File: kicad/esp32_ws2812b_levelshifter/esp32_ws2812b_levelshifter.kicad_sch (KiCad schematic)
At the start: 8 parts, among them J1 ESP32, J2 WS2812B, J3 PWR_5V, U1 SN74HCT245

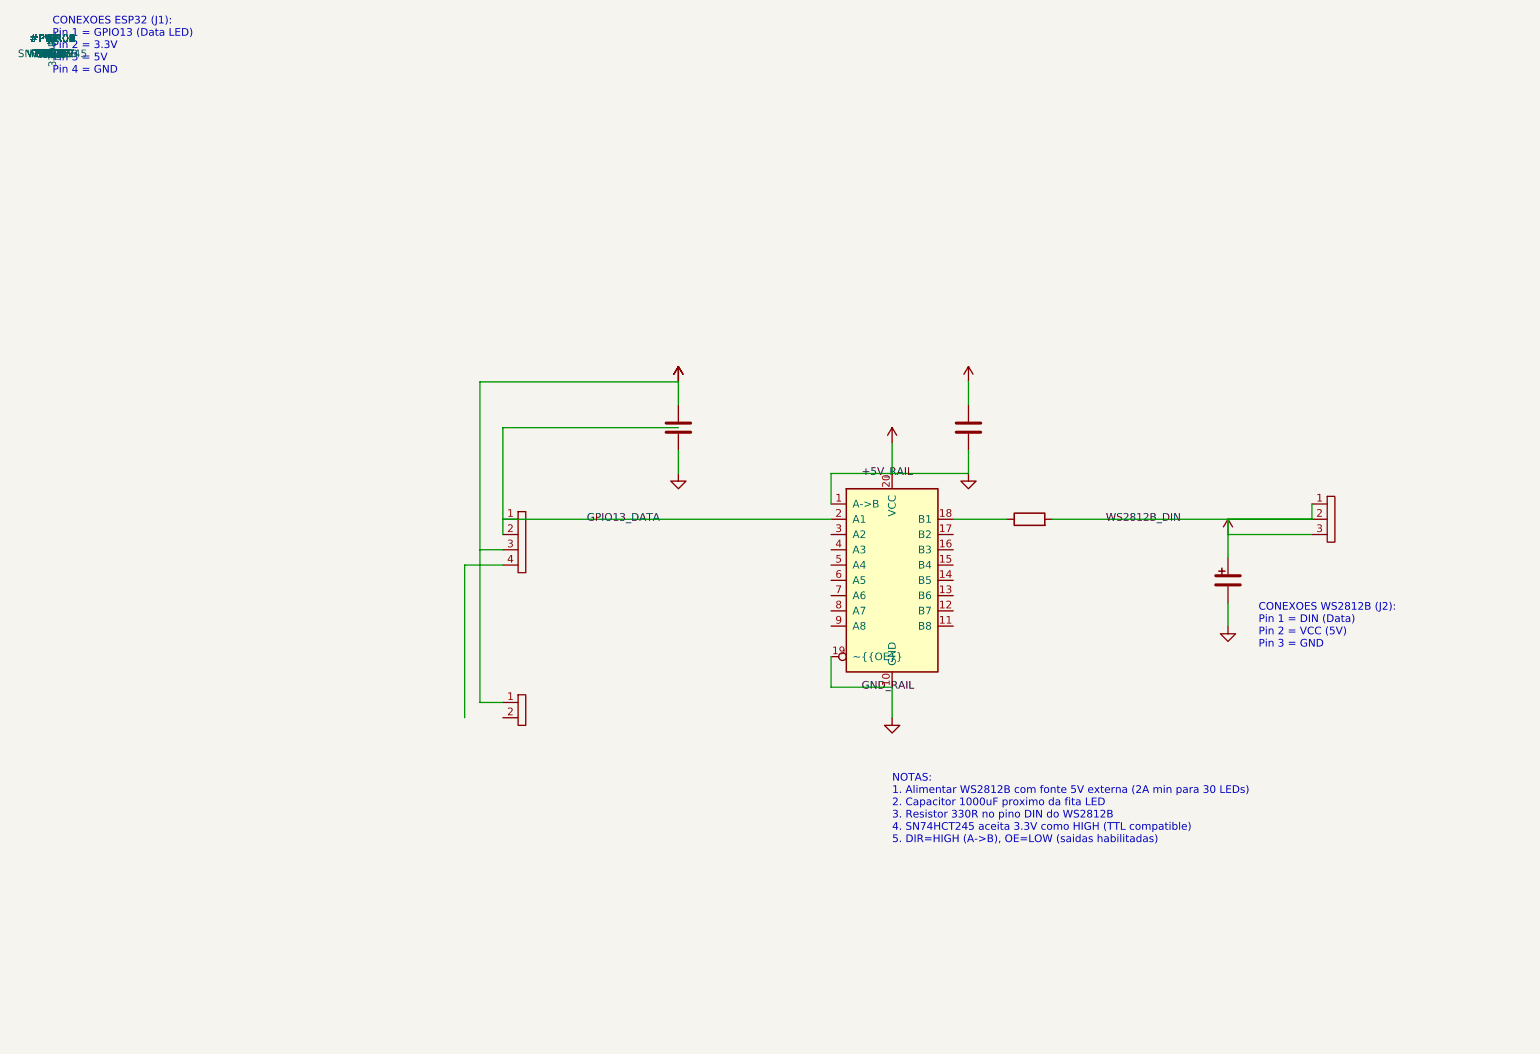
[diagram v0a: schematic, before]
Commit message: refactor: update to SN74HCT125 (DIP-14) per user schematic
- Replace SN74HCT245 (DIP-20) with SN74HCT125 (DIP-14, quad buffer)
- All ~OE pins tied to GND (outputs always enabled)
- Channel 1: GPIO13 -> 1A (pin2) -> 1Y (pin3) -> R1 -> WS2812B DIN
- Resistor changed from 330R to 62-100R per reference schematic
- 100nF bypass cap between VCC (pin14) and GND (pin7)
- PCB reduced to 40x30mm (smaller IC footprint)
- Updated BOM and documentation

Co-Authored-By: josefrizi@gmail.com <josefrizi@gmail.com>
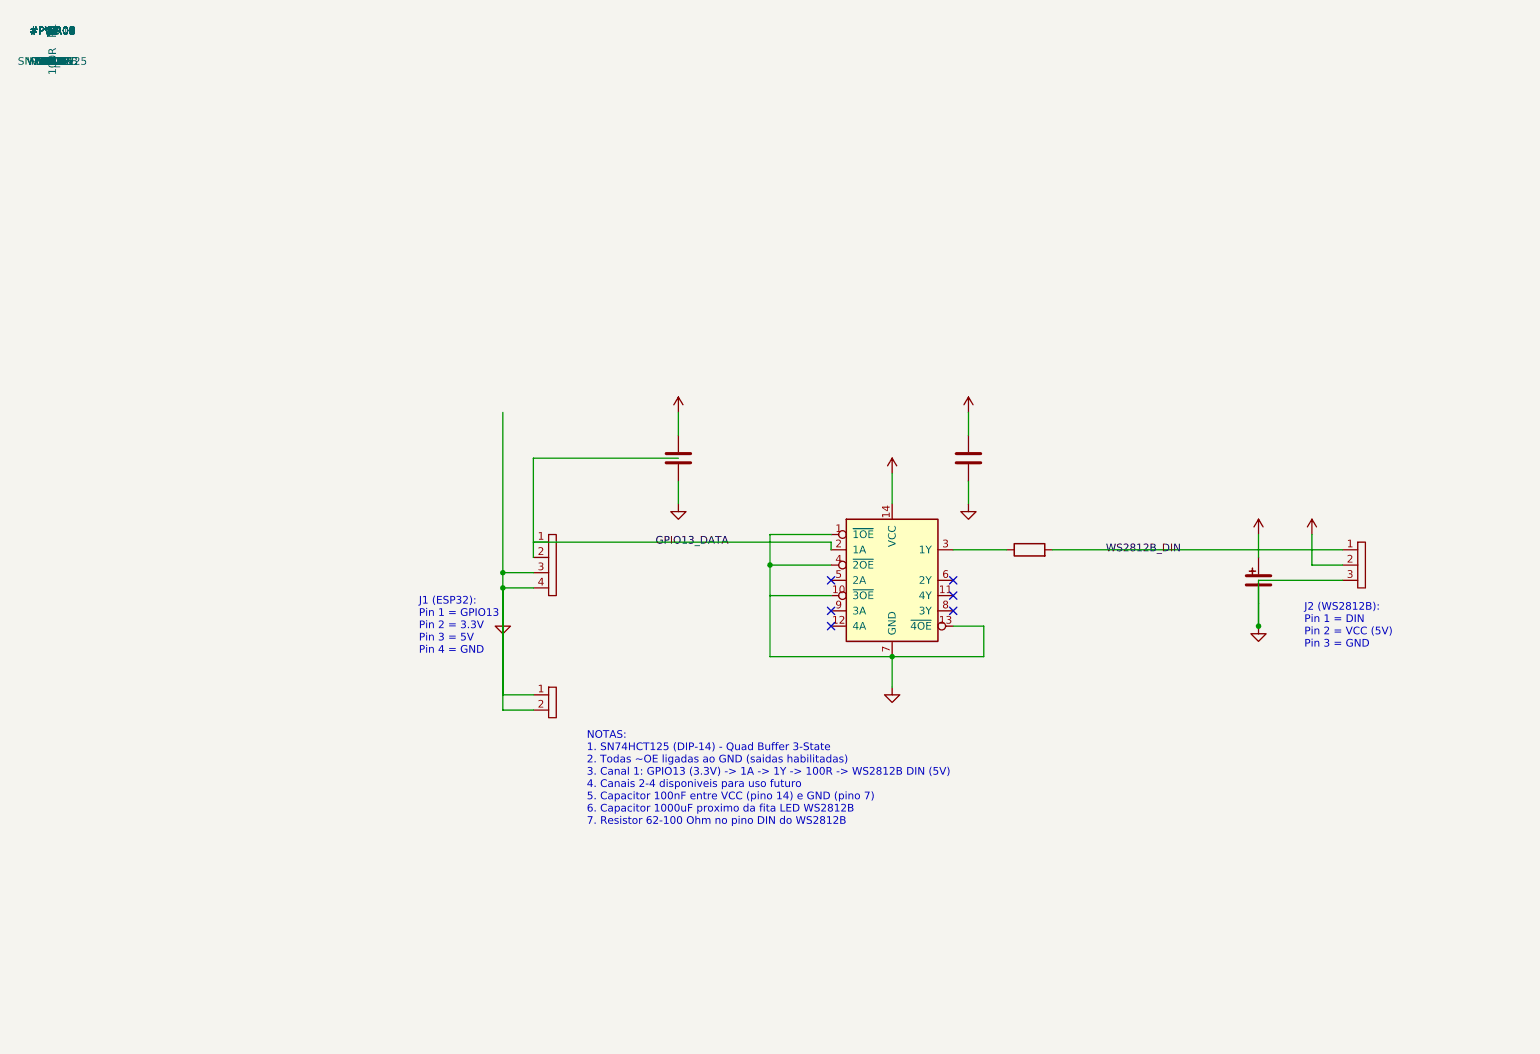
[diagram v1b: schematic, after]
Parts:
- removed U1: SN74HCT245, symbol 74xx:74HCT245
- added U1: SN74HCT125, symbol 74xx:74HCT125
- R1: value 330R -> 100R
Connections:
- net +3V3: no longer C1.1, C1.2, C2.1, C2.2, C3.2, J1.3 (Pin_3), J2.1 (Pin_1), J2.2 (Pin_2), J2.3 (Pin_3), J3.1 (Pin_1), R1.2
- net GPIO13_DATA: now also U1.2 (1A)
- net GND: now reaches J3.2 (Pin_2)
- net GND: now also C1.2, C2.2, C3.2, J1.3 (Pin_3), J1.4 (Pin_4), J2.3 (Pin_3), J3.1 (Pin_1), U1.1 (~{1OE}), U1.10 (~{3OE}), U1.13 (~{4OE}), U1.4 (~{2OE}), U1.7 (GND)
- net at R1.1: now also U1.3 (1Y)
- new net +5V: C1.1, C2.1, J2.2 (Pin_2), U1.14 (VCC)
- new net WS2812B_DIN: J2.1 (Pin_1), R1.2
- no-connect marks 0 -> 6
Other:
- note added: "J1 (ESP32): Pin 1 = GPIO13 Pin 2 = 3.3V Pin 3 = 5V Pin 4 = GND"
- note added: "J2 (WS2812B): Pin 1 = DIN Pin 2 = VCC (5V) Pin 3 = GND"
- note added: "NOTAS: 1. SN74HCT125 (DIP-14) - Quad Buffer 3-State 2. Todas ~OE ligadas ao GND (saidas habilitadas) 3. Canal 1: GPIO13 (3.3V) -> 1A -> 1Y -> 100R -> WS2812B DIN (5V) 4. Canais 2-4 disponiveis para uso futuro 5. Capacitor 100nF entre VCC (pino 14) e GND (pino 7) 6. Capacitor 1000uF proximo da fita LED WS2812B 7. Resistor 62-100 Ohm no pino DIN do WS2812B"
- note removed: "CONEXOES ESP32 (J1): Pin 1 = GPIO13 (Data LED) Pin 2 = 3.3V Pin 3 = 5V Pin 4 = GND"
- note removed: "CONEXOES WS2812B (J2): Pin 1 = DIN (Data) Pin 2 = VCC (5V) Pin 3 = GND"
- note removed: "NOTAS: 1. Alimentar WS2812B com fonte 5V externa (2A min para 30 LEDs) 2. Capacitor 1000uF proximo da fita LED 3. Resistor 330R no pino DIN do WS2812B 4. SN74HCT245 aceita 3.3V como HIGH (TTL compatible) 5. DIR=HIGH (A->B), OE=LOW (saidas habilitadas)"
- title: ESP32 + SN74HCT245 Level Shifter para WS2812B -> ESP32 + SN74HCT125 Level Shifter para WS2812B

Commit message: fix: use official KiCad multi-unit symbol format for SN74HCT125
- Symbol now uses 5 units (4 gates + power) matching KiCad 74xx library format
- Each gate drawn as triangle buffer with ~OE, A input, Y output
- Unit 5 contains VCC (pin 14) and GND (pin 7) in rectangle
- Fixes symbol loading issue in KiCad 10
- Matches official 74LS125 symbol structure (74HCT125 extends 74LS125)

Co-Authored-By: josefrizi@gmail.com <josefrizi@gmail.com>
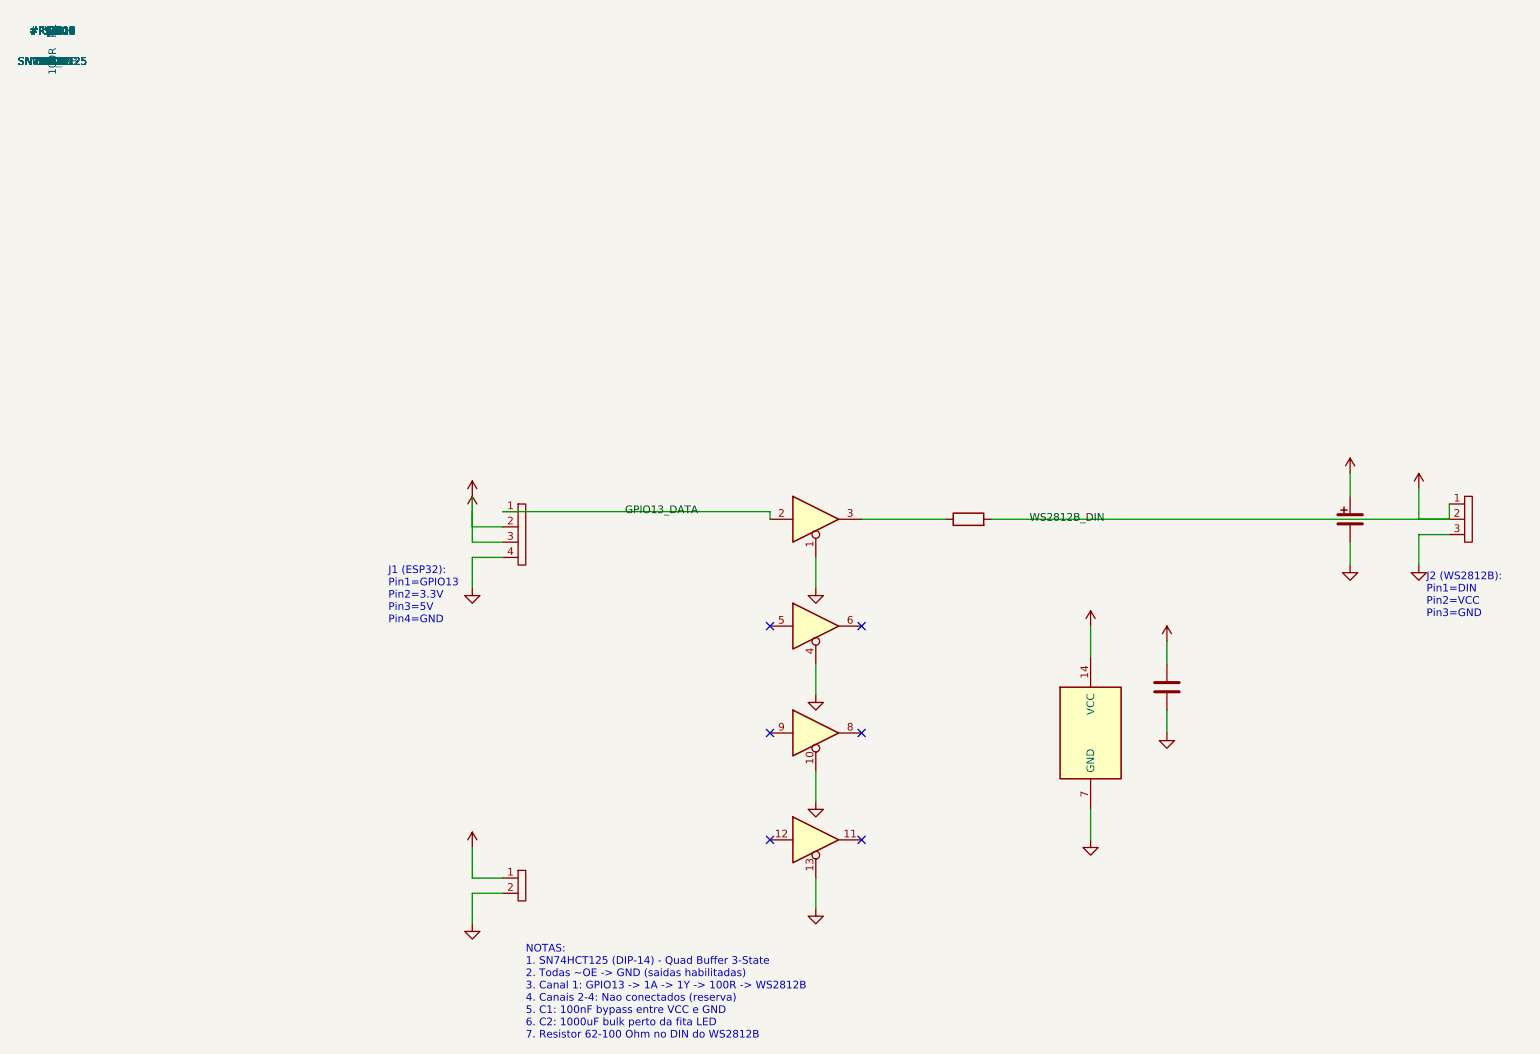
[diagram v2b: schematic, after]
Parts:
- removed C3: 100nF, symbol Device:C
- added unit 4 of U1
- added unit 5 of U1
- added unit 3 of U1
- added unit 2 of U1
- J3: value PWR_5V -> PWR_IN
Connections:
- net WS2812B_DIN is gone; now on net +3V3: J2.1 (Pin_1), R1.2
- net +3V3: now also C1.1, C2.1, J1.2 (Pin_2), J1.3 (Pin_3), J2.2 (Pin_2), J3.1 (Pin_1), U1.14 (VCC)
- net GND: now also U1.10, U1.13, U1.4, U1.7 (GND); no longer J1.3 (Pin_3), J3.1 (Pin_1), U1.10 (~{3OE}), U1.13 (~{4OE}), U1.4 (~{2OE}), U1.7 (GND)
- removed net +5V: C1.1, C2.1, J2.2 (Pin_2), U1.14 (VCC)
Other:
- note added: "J1 (ESP32): Pin1=GPIO13 Pin2=3.3V Pin3=5V Pin4=GND"
- note added: "J2 (WS2812B): Pin1=DIN Pin2=VCC Pin3=GND"
- note added: "NOTAS: 1. SN74HCT125 (DIP-14) - Quad Buffer 3-State 2. Todas ~OE -> GND (saidas habilitadas) 3. Canal 1: GPIO13 -> 1A -> 1Y -> 100R -> WS2812B 4. Canais 2-4: Nao conectados (reserva) 5. C1: 100nF bypass entre VCC e GND 6. C2: 1000uF bulk perto da fita LED 7. Resistor 62-100 Ohm no DIN do WS2812B"
- note removed: "J1 (ESP32): Pin 1 = GPIO13 Pin 2 = 3.3V Pin 3 = 5V Pin 4 = GND"
- note removed: "J2 (WS2812B): Pin 1 = DIN Pin 2 = VCC (5V) Pin 3 = GND"
- note removed: "NOTAS: 1. SN74HCT125 (DIP-14) - Quad Buffer 3-State 2. Todas ~OE ligadas ao GND (saidas habilitadas) 3. Canal 1: GPIO13 (3.3V) -> 1A -> 1Y -> 100R -> WS2812B DIN (5V) 4. Canais 2-4 disponiveis para uso futuro 5. Capacitor 100nF entre VCC (pino 14) e GND (pino 7) 6. Capacitor 1000uF proximo da fita LED WS2812B 7. Resistor 62-100 Ohm no pino DIN do WS2812B"

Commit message: fix: single-unit DIP-14 block symbol for SN74HCT125
- All 14 pins visible in one rectangle block (DIP-14 layout)
- Left side: pins 1-7 (~1OE, 1A, 1Y, ~2OE, 2A, 2Y, GND)
- Right side: pins 14-8 (VCC, ~4OE, 4A, 4Y, ~3OE, 3A, 3Y)
- Pin names with overbar notation: ~{1OE}, ~{2OE}, ~{3OE}, ~{4OE}
- IC shows as complete DIP-14 package in schematic

Co-Authored-By: josefrizi@gmail.com <josefrizi@gmail.com>
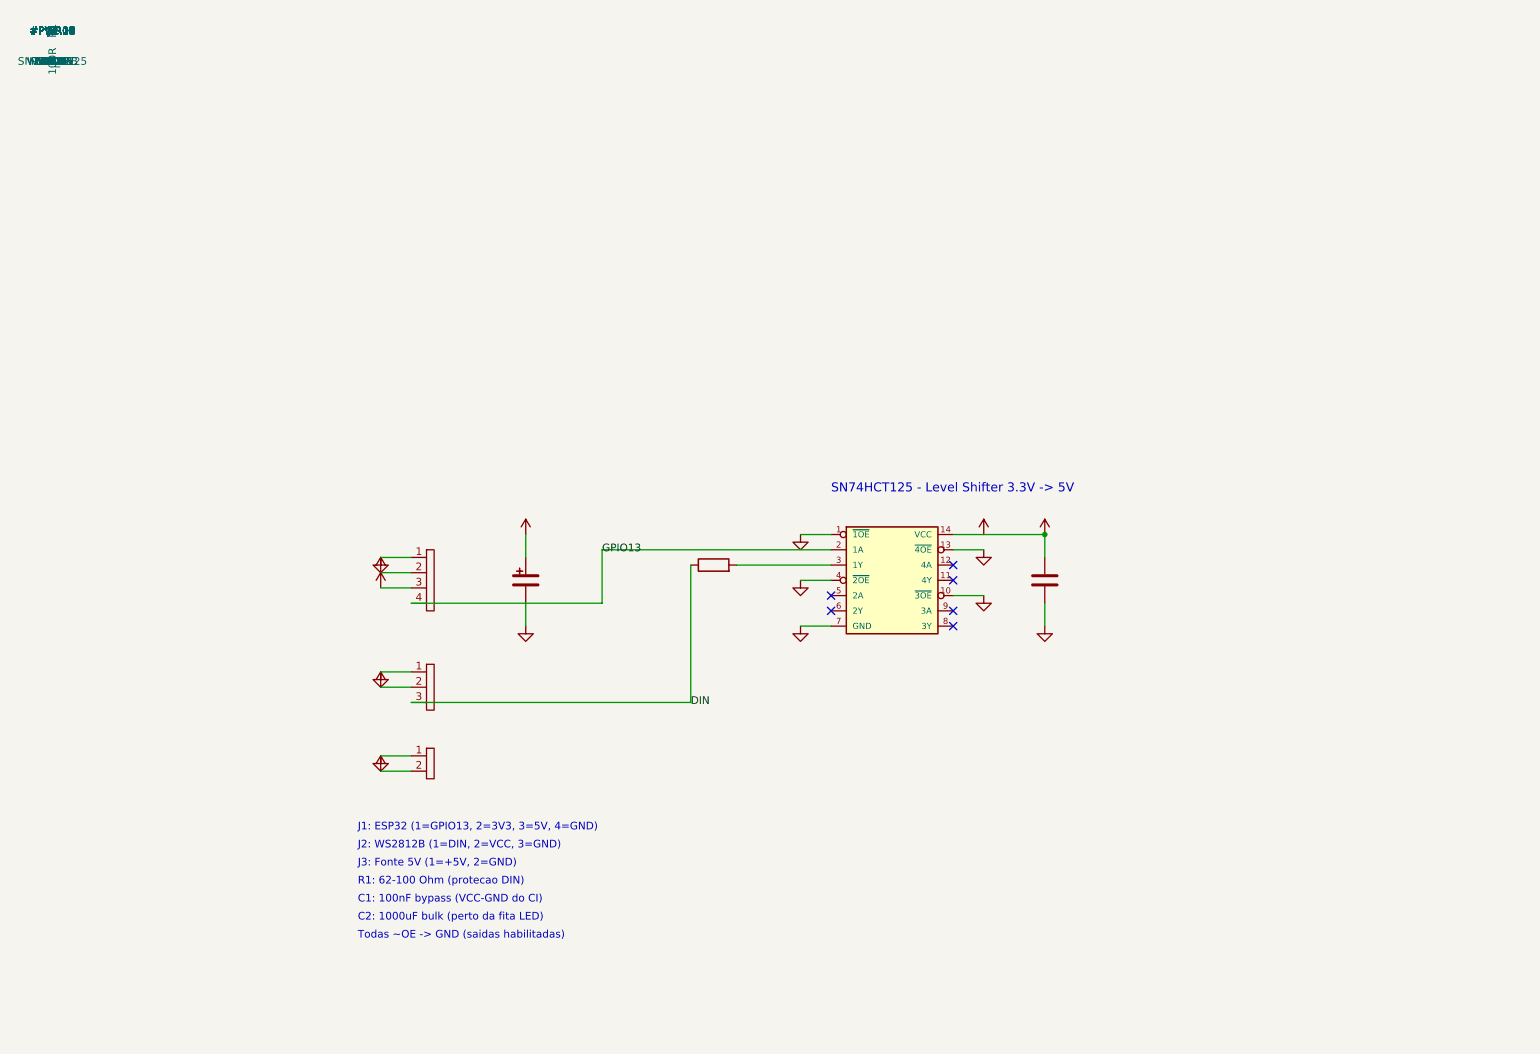
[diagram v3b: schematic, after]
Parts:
- removed unit 4 of U1
- removed unit 5 of U1
- removed unit 3 of U1
- removed unit 2 of U1
- C1: footprint (none) -> Capacitor_THT:C_Disc_D5.0mm_W2.5mm_P2.54mm
- C2: footprint (none) -> Capacitor_THT:CP_Radial_D8.0mm_P3.50mm
- J1: footprint (none) -> Connector_PinHeader_2.54mm:PinHeader_1x04_P2.54mm_Vertical
- J2: footprint (none) -> Connector_PinHeader_2.54mm:PinHeader_1x03_P2.54mm_Vertical
- J3: value PWR_IN -> PWR_5V; footprint (none) -> Connector_PinHeader_2.54mm:PinHeader_1x02_P2.54mm_Vertical
- R1: footprint (none) -> Resistor_THT:R_Axial_DIN0207_L6.3mm_D2.5mm_P10.16mm_Horizontal
- U1: footprint (none) -> Package_DIP:DIP-14_W7.62mm
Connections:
- net +3V3: no longer C1.1, C2.1, J1.2 (Pin_2), J2.1 (Pin_1), J2.2 (Pin_2), J3.1 (Pin_1), R1.2
- net GND: now also J1.1 (Pin_1), J2.1 (Pin_1), J3.1 (Pin_1), U1.10 (~{3OE}), U1.13 (~{4OE}), U1.4 (~{2OE}), U1.7 (GND); no longer J1.4 (Pin_4), J2.3 (Pin_3), J3.2 (Pin_2)
- net at U1.3 (1Y): now also R1.2; no longer R1.1
- net GPIO13_DATA renamed GPIO13
- net GPIO13: now also J1.4 (Pin_4); no longer J1.1 (Pin_1)
- new net +5V: C1.1, C2.1, J1.2 (Pin_2), J2.2 (Pin_2), J3.2 (Pin_2), U1.14 (VCC)
- new net DIN: J2.3 (Pin_3), R1.1
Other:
- note added: "C1: 100nF bypass (VCC-GND do CI)"
- note added: "C2: 1000uF bulk (perto da fita LED)"
- note added: "J1: ESP32 (1=GPIO13, 2=3V3, 3=5V, 4=GND)"
- note added: "J2: WS2812B (1=DIN, 2=VCC, 3=GND)"
- note added: "J3: Fonte 5V (1=+5V, 2=GND)"
- note added: "R1: 62-100 Ohm (protecao DIN)"
- note added: "SN74HCT125 - Level Shifter 3.3V -> 5V"
- note added: "Todas ~OE -> GND (saidas habilitadas)"
- note removed: "J1 (ESP32): Pin1=GPIO13 Pin2=3.3V Pin3=5V Pin4=GND"
- note removed: "J2 (WS2812B): Pin1=DIN Pin2=VCC Pin3=GND"
- note removed: "NOTAS: 1. SN74HCT125 (DIP-14) - Quad Buffer 3-State 2. Todas ~OE -> GND (saidas habilitadas) 3. Canal 1: GPIO13 -> 1A -> 1Y -> 100R -> WS2812B 4. Canais 2-4: Nao conectados (reserva) 5. C1: 100nF bypass entre VCC e GND 6. C2: 1000uF bulk perto da fita LED 7. Resistor 62-100 Ohm no DIN do WS2812B"
